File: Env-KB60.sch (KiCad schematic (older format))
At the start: 129 parts, among them U1 Pico

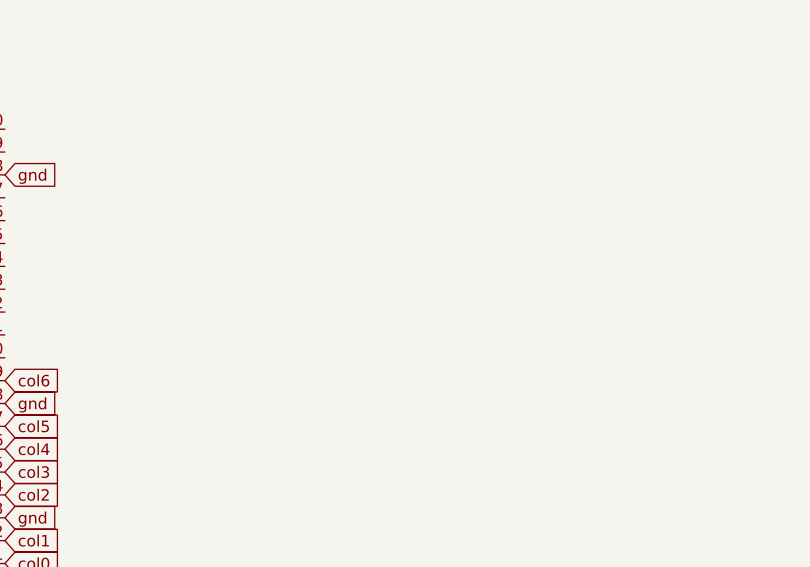
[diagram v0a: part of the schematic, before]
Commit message: Added 6*M2 Mount holes
There is one mount hole in each corner and also a couple along the center line of the board, one below the space bar and the other between the top two rows.
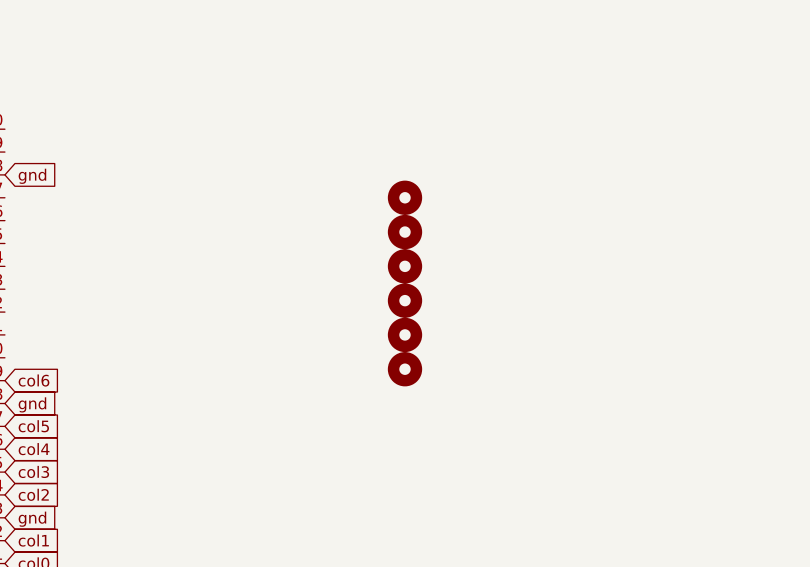
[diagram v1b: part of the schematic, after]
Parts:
- added H1, H2, H3, H4, H5, H6: MountingHole, MountingHole:MountingHole_2.2mm_M2, symbol Mechanical:MountingHole
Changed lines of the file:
@@
 	1150 4150 1350 4150
 Connection ~ 1350 4150
+$Comp
+L Mechanical:MountingHole H1
+U 1 1 6076A53B
+P 7300 6600
+F 0 "H1" H 7400 6646 50  0001 L CNN
+F 1 "MountingHole" H 7400 6555 50  0001 L CNN
+F 2 "MountingHole:MountingHole_2.2mm_M2" H 7300 6600 50  0001 C CNN
+F 3 "~" H 7300 6600 50  0001 C CNN
+	1    7300 6600
+	1    0    0    -1
+$EndComp
+$Comp
+L Mechanical:MountingHole H2
+U 1 1 6076BA3D
+P 7300 6750
+F 0 "H2" H 7400 6796 50  0001 L CNN
+F 1 "MountingHole" H 7400 6705 50  0001 L CNN
+F 2 "MountingHole:MountingHole_2.2mm_M2" H 7300 6750 50  0001 C CNN
+F 3 "~" H 7300 6750 50  0001 C CNN
+	1    7300 6750
+	1    0    0    -1
+$EndComp
+$Comp
+L Mechanical:MountingHole H3
+U 1 1 6077D67F
+P 7300 6900
+F 0 "H3" H 7400 6946 50  0001 L CNN
+F 1 "MountingHole" H 7400 6855 50  0001 L CNN
+F 2 "MountingHole:MountingHole_2.2mm_M2" H 7300 6900 50  0001 C CNN
+F 3 "~" H 7300 6900 50  0001 C CNN
+	1    7300 6900
+	1    0    0    -1
+$EndComp
+$Comp
+L Mechanical:MountingHole H4
+U 1 1 6078F20E
+P 7300 7050
+F 0 "H4" H 7400 7096 50  0001 L CNN
+F 1 "MountingHole" H 7400 7005 50  0001 L CNN
+F 2 "MountingHole:MountingHole_2.2mm_M2" H 7300 7050 50  0001 C CNN
+F 3 "~" H 7300 7050 50  0001 C CNN
+	1    7300 7050
+	1    0    0    -1
+$EndComp
+$Comp
+L Mechanical:MountingHole H5
+U 1 1 607A12FF
+P 7300 7200
+F 0 "H5" H 7400 7246 50  0001 L CNN
+F 1 "MountingHole" H 7400 7155 50  0001 L CNN
+F 2 "MountingHole:MountingHole_2.2mm_M2" H 7300 7200 50  0001 C CNN
+F 3 "~" H 7300 7200 50  0001 C CNN
+	1    7300 7200
+	1    0    0    -1
+$EndComp
+$Comp
+L Mechanical:MountingHole H6
+U 1 1 607B2F46
+P 7300 7350
+F 0 "H6" H 7400 7396 50  0001 L CNN
+F 1 "MountingHole" H 7400 7305 50  0001 L CNN
+F 2 "MountingHole:MountingHole_2.2mm_M2" H 7300 7350 50  0001 C CNN
+F 3 "~" H 7300 7350 50  0001 C CNN
+	1    7300 7350
+	1    0    0    -1
+$EndComp
 $EndSCHEMATC

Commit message: Re-Doing this PCB
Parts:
- removed D_1, D_28: D, Diode_THT:D_DO-35_SOD27_P7.62mm_Horizontal, symbol Device:D_Small
- removed H1, H2, H3, H4, H5, H6: MountingHole, MountingHole:MountingHole_2.2mm_M2, symbol Mechanical:MountingHole
- removed K_28: KEYSW, MX_Only:MXOnly-1.5U-NoLED, symbol MX_Alps_Hybrid:MX-NoLED
- removed K_42: KEYSW, MX_Only:MXOnly-2.25U-NoLED, symbol MX_Alps_Hybrid:MX-NoLED
- removed K_44: KEYSW, MX_Only:MXOnly-2.25U-ReversedStabilizers-NoLED, symbol MX_Alps_Hybrid:MX-NoLED
- removed U1: Pico, MCU_RaspberryPi_and_Boards:RPi_Pico_SMD_TH, symbol MCU_RaspberryPi_and_Boards:Pico
- added D_0: D, Diode_SMD:D_SOD-123, symbol Device:D_Small
- D_1: renamed from D_2; footprint Diode_THT:D_DO-35_SOD27_P7.62mm_Horizontal -> Diode_SMD:D_SOD-123
- D_10: renamed from D_11; footprint Diode_THT:D_DO-35_SOD27_P7.62mm_Horizontal -> Diode_SMD:D_SOD-123
- D_11: renamed from D_12; footprint Diode_THT:D_DO-35_SOD27_P7.62mm_Horizontal -> Diode_SMD:D_SOD-123
- D_12: renamed from D_13; footprint Diode_THT:D_DO-35_SOD27_P7.62mm_Horizontal -> Diode_SMD:D_SOD-123
- D_13: renamed from D_14; footprint Diode_THT:D_DO-35_SOD27_P7.62mm_Horizontal -> Diode_SMD:D_SOD-123
- D_14: renamed from D_15; footprint Diode_THT:D_DO-35_SOD27_P7.62mm_Horizontal -> Diode_SMD:D_SOD-123
- D_15: renamed from D_16; footprint Diode_THT:D_DO-35_SOD27_P7.62mm_Horizontal -> Diode_SMD:D_SOD-123
- D_16: renamed from D_17; footprint Diode_THT:D_DO-35_SOD27_P7.62mm_Horizontal -> Diode_SMD:D_SOD-123
- D_17: renamed from D_18; footprint Diode_THT:D_DO-35_SOD27_P7.62mm_Horizontal -> Diode_SMD:D_SOD-123
- D_18: renamed from D_19; footprint Diode_THT:D_DO-35_SOD27_P7.62mm_Horizontal -> Diode_SMD:D_SOD-123
- D_19: renamed from D_20; footprint Diode_THT:D_DO-35_SOD27_P7.62mm_Horizontal -> Diode_SMD:D_SOD-123
- D_2: renamed from D_3; footprint Diode_THT:D_DO-35_SOD27_P7.62mm_Horizontal -> Diode_SMD:D_SOD-123
- D_20: renamed from D_21; footprint Diode_THT:D_DO-35_SOD27_P7.62mm_Horizontal -> Diode_SMD:D_SOD-123
- D_21: renamed from D_22; footprint Diode_THT:D_DO-35_SOD27_P7.62mm_Horizontal -> Diode_SMD:D_SOD-123
- D_22: renamed from D_23; footprint Diode_THT:D_DO-35_SOD27_P7.62mm_Horizontal -> Diode_SMD:D_SOD-123
- D_23: renamed from D_24; footprint Diode_THT:D_DO-35_SOD27_P7.62mm_Horizontal -> Diode_SMD:D_SOD-123
- D_24: renamed from D_25; footprint Diode_THT:D_DO-35_SOD27_P7.62mm_Horizontal -> Diode_SMD:D_SOD-123
- D_25: renamed from D_26; footprint Diode_THT:D_DO-35_SOD27_P7.62mm_Horizontal -> Diode_SMD:D_SOD-123
- D_26: renamed from D_27; footprint Diode_THT:D_DO-35_SOD27_P7.62mm_Horizontal -> Diode_SMD:D_SOD-123
- D_27: renamed from D_42; footprint Diode_THT:D_DO-35_SOD27_P7.62mm_Horizontal -> Diode_SMD:D_SOD-123
- D_28: renamed from D_29; footprint Diode_THT:D_DO-35_SOD27_P7.62mm_Horizontal -> Diode_SMD:D_SOD-123
- D_29: renamed from D_30; footprint Diode_THT:D_DO-35_SOD27_P7.62mm_Horizontal -> Diode_SMD:D_SOD-123
- D_3: renamed from D_4; footprint Diode_THT:D_DO-35_SOD27_P7.62mm_Horizontal -> Diode_SMD:D_SOD-123
- D_30: renamed from D_31; footprint Diode_THT:D_DO-35_SOD27_P7.62mm_Horizontal -> Diode_SMD:D_SOD-123
- D_31: renamed from D_32; footprint Diode_THT:D_DO-35_SOD27_P7.62mm_Horizontal -> Diode_SMD:D_SOD-123
- D_32: renamed from D_33; footprint Diode_THT:D_DO-35_SOD27_P7.62mm_Horizontal -> Diode_SMD:D_SOD-123
- D_33: renamed from D_34; footprint Diode_THT:D_DO-35_SOD27_P7.62mm_Horizontal -> Diode_SMD:D_SOD-123
- D_34: renamed from D_35; footprint Diode_THT:D_DO-35_SOD27_P7.62mm_Horizontal -> Diode_SMD:D_SOD-123
- D_35: renamed from D_36; footprint Diode_THT:D_DO-35_SOD27_P7.62mm_Horizontal -> Diode_SMD:D_SOD-123
- D_36: renamed from D_37; footprint Diode_THT:D_DO-35_SOD27_P7.62mm_Horizontal -> Diode_SMD:D_SOD-123
- D_37: renamed from D_38; footprint Diode_THT:D_DO-35_SOD27_P7.62mm_Horizontal -> Diode_SMD:D_SOD-123
- D_38: renamed from D_39; footprint Diode_THT:D_DO-35_SOD27_P7.62mm_Horizontal -> Diode_SMD:D_SOD-123
- D_39: renamed from D_40; footprint Diode_THT:D_DO-35_SOD27_P7.62mm_Horizontal -> Diode_SMD:D_SOD-123
- D_4: renamed from D_5; footprint Diode_THT:D_DO-35_SOD27_P7.62mm_Horizontal -> Diode_SMD:D_SOD-123
- D_40: renamed from D_41; footprint Diode_THT:D_DO-35_SOD27_P7.62mm_Horizontal -> Diode_SMD:D_SOD-123
- D_41: renamed from D_43; footprint Diode_THT:D_DO-35_SOD27_P7.62mm_Horizontal -> Diode_SMD:D_SOD-123
- D_42: renamed from D_44; footprint Diode_THT:D_DO-35_SOD27_P7.62mm_Horizontal -> Diode_SMD:D_SOD-123
- D_43: renamed from D_45; footprint Diode_THT:D_DO-35_SOD27_P7.62mm_Horizontal -> Diode_SMD:D_SOD-123
- D_44: renamed from D_46; footprint Diode_THT:D_DO-35_SOD27_P7.62mm_Horizontal -> Diode_SMD:D_SOD-123
- D_45: renamed from D_47; footprint Diode_THT:D_DO-35_SOD27_P7.62mm_Horizontal -> Diode_SMD:D_SOD-123
- D_46: renamed from D_48; footprint Diode_THT:D_DO-35_SOD27_P7.62mm_Horizontal -> Diode_SMD:D_SOD-123
- D_47: renamed from D_49; footprint Diode_THT:D_DO-35_SOD27_P7.62mm_Horizontal -> Diode_SMD:D_SOD-123
- D_48: renamed from D_50; footprint Diode_THT:D_DO-35_SOD27_P7.62mm_Horizontal -> Diode_SMD:D_SOD-123
- D_49: renamed from D_51; footprint Diode_THT:D_DO-35_SOD27_P7.62mm_Horizontal -> Diode_SMD:D_SOD-123
- D_5: renamed from D_6; footprint Diode_THT:D_DO-35_SOD27_P7.62mm_Horizontal -> Diode_SMD:D_SOD-123
- D_50: renamed from D_52; footprint Diode_THT:D_DO-35_SOD27_P7.62mm_Horizontal -> Diode_SMD:D_SOD-123
- D_51: renamed from D_53; footprint Diode_THT:D_DO-35_SOD27_P7.62mm_Horizontal -> Diode_SMD:D_SOD-123
- D_52: renamed from D_54; footprint Diode_THT:D_DO-35_SOD27_P7.62mm_Horizontal -> Diode_SMD:D_SOD-123
- D_53: renamed from D_55; footprint Diode_THT:D_DO-35_SOD27_P7.62mm_Horizontal -> Diode_SMD:D_SOD-123
- D_54: renamed from D_56; footprint Diode_THT:D_DO-35_SOD27_P7.62mm_Horizontal -> Diode_SMD:D_SOD-123
- D_55: renamed from D_57; footprint Diode_THT:D_DO-35_SOD27_P7.62mm_Horizontal -> Diode_SMD:D_SOD-123
- D_56: renamed from D_58; footprint Diode_THT:D_DO-35_SOD27_P7.62mm_Horizontal -> Diode_SMD:D_SOD-123
- D_57: renamed from D_59; footprint Diode_THT:D_DO-35_SOD27_P7.62mm_Horizontal -> Diode_SMD:D_SOD-123
- D_58: renamed from D_60; footprint Diode_THT:D_DO-35_SOD27_P7.62mm_Horizontal -> Diode_SMD:D_SOD-123
- D_59: renamed from D_61; footprint Diode_THT:D_DO-35_SOD27_P7.62mm_Horizontal -> Diode_SMD:D_SOD-123
- D_6: renamed from D_7; footprint Diode_THT:D_DO-35_SOD27_P7.62mm_Horizontal -> Diode_SMD:D_SOD-123
- D_60: renamed from D_62; footprint Diode_THT:D_DO-35_SOD27_P7.62mm_Horizontal -> Diode_SMD:D_SOD-123
- D_61: renamed from D_63; footprint Diode_THT:D_DO-35_SOD27_P7.62mm_Horizontal -> Diode_SMD:D_SOD-123
- D_7: renamed from D_8; footprint Diode_THT:D_DO-35_SOD27_P7.62mm_Horizontal -> Diode_SMD:D_SOD-123
- D_8: renamed from D_9; footprint Diode_THT:D_DO-35_SOD27_P7.62mm_Horizontal -> Diode_SMD:D_SOD-123
- D_9: renamed from D_10; footprint Diode_THT:D_DO-35_SOD27_P7.62mm_Horizontal -> Diode_SMD:D_SOD-123
- K_57: renamed from K_61; footprint MX_Only:MXOnly-6.25U-NoLED -> MX_Only:MXOnly-6.25U-ReversedStabilizers-NoLED
- renumbered K_1 to K_0, K_2 to K_1, K_11 to K_10, K_12 to K_11, K_13 to K_12, K_14 to K_13, K_15 to K_14, K_16 to K_15, K_17 to K_16, K_18 to K_17, K_19 to K_18, K_20 to K_19, K_3 to K_2, K_21 to K_20, K_22 to K_21, K_23 to K_22, K_24 to K_23, K_25 to K_24, K_26 to K_25, K_27 to K_26, K_43 to K_27, K_29 to K_28, K_30 to K_29, K_4 to K_3, K_31 to K_30, K_32 to K_31, K_33 to K_32, K_34 to K_33, K_35 to K_34, K_36 to K_35, K_37 to K_36, K_38 to K_37, K_39 to K_38, K_40 to K_39, K_5 to K_4, K_41 to K_40, K_45 to K_41, K_46 to K_42, K_47 to K_43, K_48 to K_44, K_49 to K_45, K_50 to K_46, K_51 to K_47, K_52 to K_48, K_53 to K_49, K_6 to K_5, K_54 to K_50, K_55 to K_51, K_56 to K_52, K_57 to K_53, K_58 to K_54, K_59 to K_55, K_60 to K_56, K_62 to K_58, K_63 to K_59, K_7 to K_6, K_64 to K_60, K_65 to K_61, K_8 to K_7, K_9 to K_8, K_10 to K_9
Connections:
- net row0: now also D_0.1 (K)
- net at K_0.2 (ROW): now also D_0.2 (A)
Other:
- note removed: "This definitely doesnt\nlook hacky right?"
- note removed: "This is Ansi Backslash"

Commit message: Added Main trace array
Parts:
- added U1: Pico, RPi_Pico:RPi_Pico_SMD_TH, symbol MCU_RaspberryPi_and_Boards:Pico
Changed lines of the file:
@@
 Wire Wire Line
 	15800 950  15800 2950
+$Comp
+L MCU_RaspberryPi_and_Boards:Pico U1
+U 1 1 6083B244
+P 5150 7900
+F 0 "U1" H 5150 9115 50  0000 C CNN
+F 1 "Pico" H 5150 9024 50  0000 C CNN
+F 2 "RPi_Pico:RPi_Pico_SMD_TH" V 5150 7900 50  0001 C CNN
+F 3 "" H 5150 7900 50  0001 C CNN
+	1    5150 7900
+	1    0    0    -1
+$EndComp
 $EndSCHEMATC

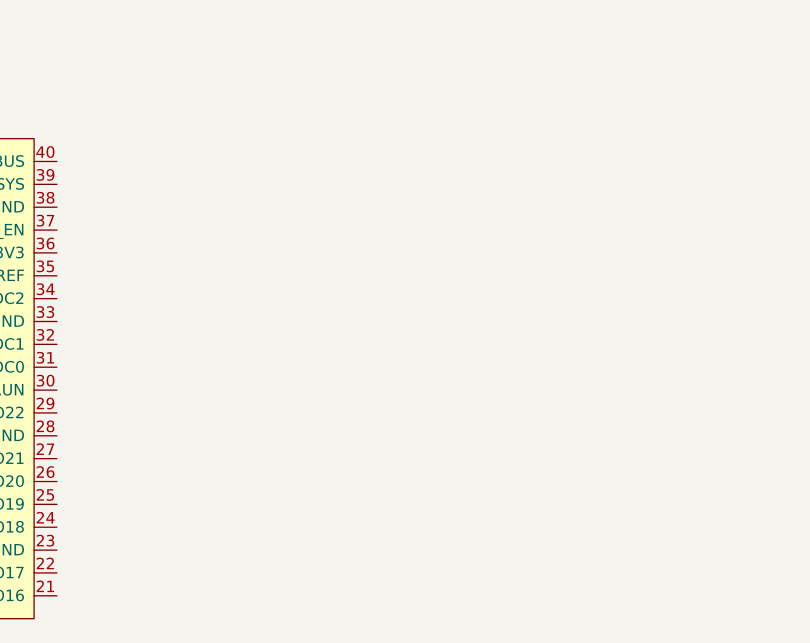
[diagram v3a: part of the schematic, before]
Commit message: Added GH60 compatible mount holes.
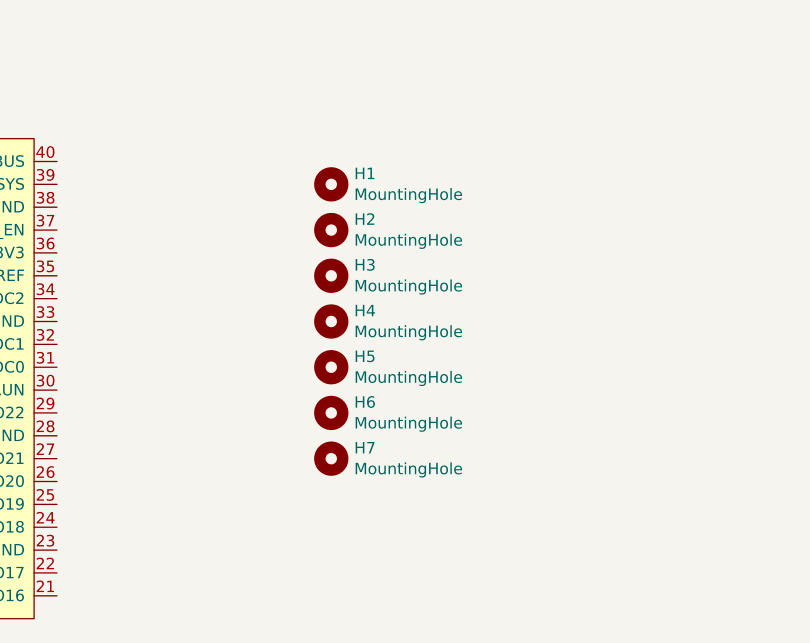
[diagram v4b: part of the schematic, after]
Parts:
- added H1, H2, H3, H4, H5, H6, H7: MountingHole, MountingHole:MountingHole_2.5mm, symbol Mechanical:MountingHole
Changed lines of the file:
@@
+	1    0    0    -1
+$EndComp
+$Comp
+L Mechanical:MountingHole H1
+U 1 1 6083D20F
+P 7050 7050
+F 0 "H1" H 7150 7096 50  0000 L CNN
+F 1 "MountingHole" H 7150 7005 50  0000 L CNN
+F 2 "MountingHole:MountingHole_2.5mm" H 7050 7050 50  0001 C CNN
+F 3 "~" H 7050 7050 50  0001 C CNN
+	1    7050 7050
+	1    0    0    -1
+$EndComp
+$Comp
+L Mechanical:MountingHole H2
+U 1 1 6083EAFA
+P 7050 7250
+F 0 "H2" H 7150 7296 50  0000 L CNN
+F 1 "MountingHole" H 7150 7205 50  0000 L CNN
+F 2 "MountingHole:MountingHole_2.5mm" H 7050 7250 50  0001 C CNN
+F 3 "~" H 7050 7250 50  0001 C CNN
+	1    7050 7250
+	1    0    0    -1
+$EndComp
+$Comp
+L Mechanical:MountingHole H3
+U 1 1 6084F3C0
+P 7050 7450
+F 0 "H3" H 7150 7496 50  0000 L CNN
+F 1 "MountingHole" H 7150 7405 50  0000 L CNN
+F 2 "MountingHole:MountingHole_2.5mm" H 7050 7450 50  0001 C CNN
+F 3 "~" H 7050 7450 50  0001 C CNN
+	1    7050 7450
+	1    0    0    -1
+$EndComp
+$Comp
+L Mechanical:MountingHole H4
+U 1 1 608603D5
+P 7050 7650
+F 0 "H4" H 7150 7696 50  0000 L CNN
+F 1 "MountingHole" H 7150 7605 50  0000 L CNN
+F 2 "MountingHole:MountingHole_2.5mm" H 7050 7650 50  0001 C CNN
+F 3 "~" H 7050 7650 50  0001 C CNN
+	1    7050 7650
+	1    0    0    -1
+$EndComp
+$Comp
+L Mechanical:MountingHole H5
+U 1 1 60870931
+P 7050 7850
+F 0 "H5" H 7150 7896 50  0000 L CNN
+F 1 "MountingHole" H 7150 7805 50  0000 L CNN
+F 2 "MountingHole:MountingHole_2.5mm" H 7050 7850 50  0001 C CNN
+F 3 "~" H 7050 7850 50  0001 C CNN
+	1    7050 7850
+	1    0    0    -1
+$EndComp
+$Comp
+L Mechanical:MountingHole H6
+U 1 1 60880F81
+P 7050 8050
+F 0 "H6" H 7150 8096 50  0000 L CNN
+F 1 "MountingHole" H 7150 8005 50  0000 L CNN
+F 2 "MountingHole:MountingHole_2.5mm" H 7050 8050 50  0001 C CNN
+F 3 "~" H 7050 8050 50  0001 C CNN
+	1    7050 8050
+	1    0    0    -1
+$EndComp
+$Comp
+L Mechanical:MountingHole H7
+U 1 1 60891579
+P 7050 8250
+F 0 "H7" H 7150 8296 50  0000 L CNN
+F 1 "MountingHole" H 7150 8205 50  0000 L CNN
+F 2 "MountingHole:MountingHole_2.5mm" H 7050 8250 50  0001 C CNN
+F 3 "~" H 7050 8250 50  0001 C CNN
+	1    7050 8250
 	1    0    0    -1
 $EndComp

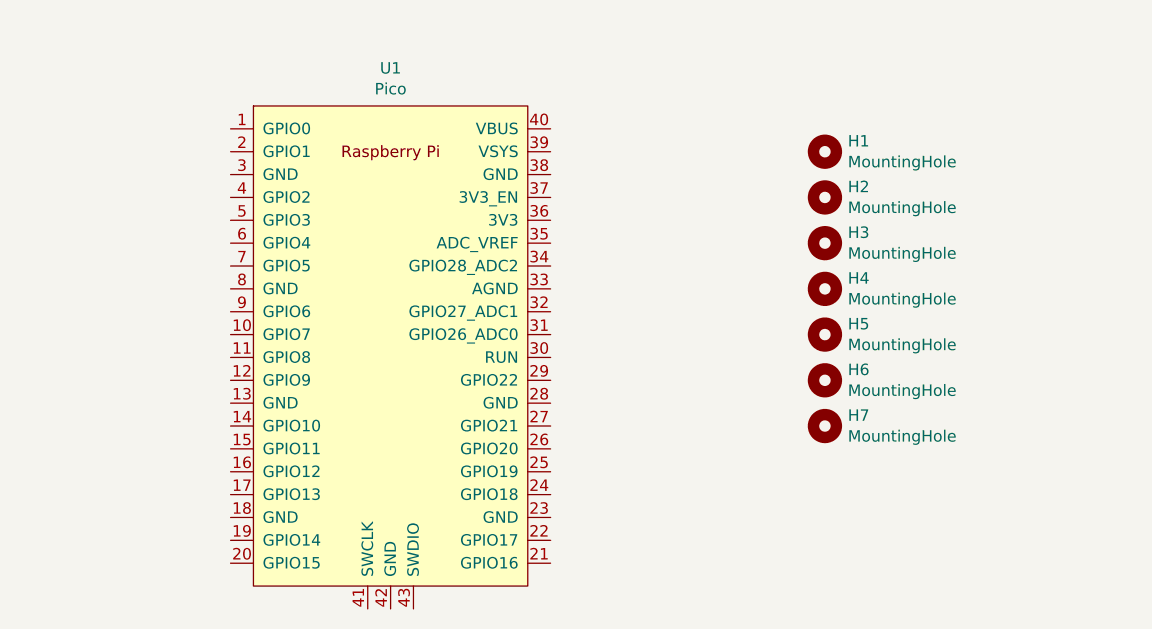
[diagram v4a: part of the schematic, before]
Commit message: added MCU and some more traces and adjustments
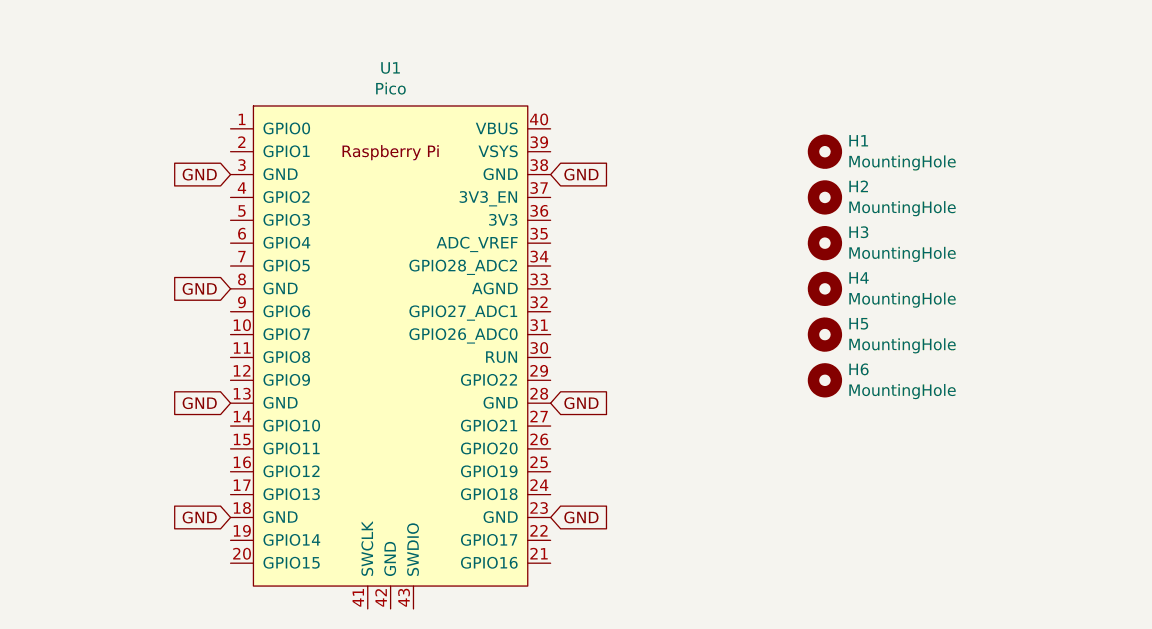
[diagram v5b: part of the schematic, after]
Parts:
- removed H7: MountingHole, MountingHole:MountingHole_2.5mm, symbol Mechanical:MountingHole
- U1: footprint RPi_Pico:RPi_Pico_SMD_TH -> MCU_RaspberryPi_and_Boards:RPi_Pico_SMD_TH
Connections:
- net GND: now reaches U1.13 (GND)
- net GND: now also U1.18 (GND), U1.23 (GND), U1.28 (GND), U1.3 (GND), U1.38 (GND), U1.8 (GND)
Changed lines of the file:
@@
 F 0 "U1" H 5150 9115 50  0000 C CNN
 F 1 "Pico" H 5150 9024 50  0000 C CNN
-F 2 "RPi_Pico:RPi_Pico_SMD_TH" V 5150 7900 50  0001 C CNN
+F 2 "MCU_RaspberryPi_and_Boards:RPi_Pico_SMD_TH" V 5150 7900 50  0001 C CNN
 F 3 "" H 5150 7900 50  0001 C CNN
 	1    5150 7900
@@
 	1    0    0    -1
 $EndComp
-$Comp
-L Mechanical:MountingHole H7
-U 1 1 60891579
-P 7050 8250
-F 0 "H7" H 7150 8296 50  0000 L CNN
-F 1 "MountingHole" H 7150 8205 50  0000 L CNN
-F 2 "MountingHole:MountingHole_2.5mm" H 7050 8250 50  0001 C CNN
-F 3 "~" H 7050 8250 50  0001 C CNN
-	1    7050 8250
-	1    0    0    -1
-$EndComp
+Text GLabel 4450 7650 0    50   Input ~ 0
+GND
+Text GLabel 4450 7150 0    50   Input ~ 0
+GND
+Text GLabel 4450 8150 0    50   Input ~ 0
+GND
+Text GLabel 4450 8650 0    50   Input ~ 0
+GND
+Text GLabel 5850 8650 2    50   Input ~ 0
+GND
+Text GLabel 5850 8150 2    50   Input ~ 0
+GND
+Text GLabel 5850 7150 2    50   Input ~ 0
+GND
 $EndSCHEMATC
